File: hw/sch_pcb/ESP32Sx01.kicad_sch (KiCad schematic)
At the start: 33 parts, among them J1 HEADER_1x03, J2 USBC_USB4105-GF-A, J3 HEADER_1x12, J4 HEADER_1x12, J5 HEADER_1x12, J6 HEADER_1x03, J7 HEADER_1x03, J8 HEADER_2x05, Q1 BC817-25, SW1 434133025816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

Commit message: Update of PCB design
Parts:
- removed J7: HEADER_1x03, Mlab_Pin_Headers:Straight_2x03, symbol MLAB_HEADER:HEADER_2x03_PARALLEL
- Y1: footprint (none) -> Mlab_XTAL:ABS07
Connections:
- net +3V3: now also J4.21, J4.22
- net GND: now also J4.1, J4.19, J4.2, J4.20, J4.23, J4.24
- net GPIO12: now also J4.3, J4.4
- net GPIO13: now also J4.5, J4.6
- net GPIO14: now also J4.7, J4.8
- net GPIO17: now also J4.10, J4.9
- net GPIO18: now also J4.11, J4.12
- net GPIO21: now also J4.13, J4.14
- net GPIO35: no longer U3.31 (SPIIO6/GPIO35/FSPID/SUBSPID)
- net GPIO36: no longer U3.32 (SPIIO7/GPIO36/FSPICLK/SUBSPICLK)
- net GPIO37: no longer U3.33 (SPIDQS/GPIO37/FSPIQ/SUBSPIQ)
- net GPIO47: now also J4.15, J4.16
- net GPIO48: now also J4.17, J4.18
- net GPIO33: no longer names the net of U3.28 (SPIIO4/GPIO33/FSPIHD/SUBSPIHD)
- net GPIO34: no longer names the net of U3.29 (SPIIO5/GPIO34/FSPICS0/SUBSPICS0)
- no-connect marks 3 -> 8

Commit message: finishing PCB design
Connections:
- net GPIO35 is gone; now on net GND: J5.1, J5.2
- net GPIO36 is gone; now on net +3V3: J5.3, J5.4
- net GPIO37 is gone; now on net GND: J5.5, J5.6
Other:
- company: (none) -> MLAB
- title: (none) -> ESP32Sx01A
- moved on the sheet: C4, C5, Y1

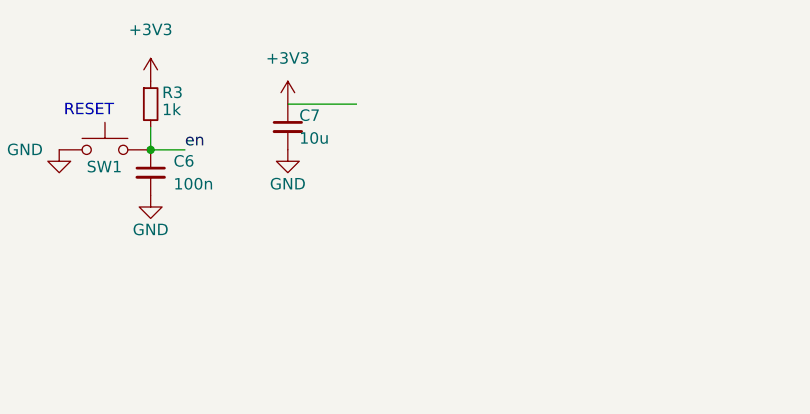
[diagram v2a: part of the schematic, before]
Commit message: move boot button
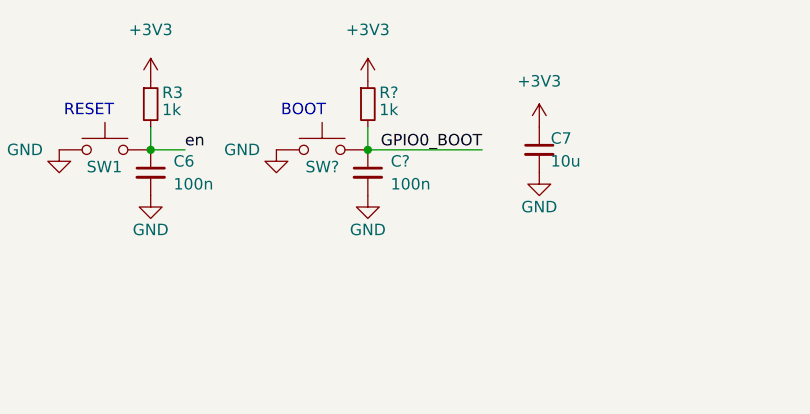
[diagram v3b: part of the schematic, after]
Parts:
- added C?: 100n, Capacitor_SMD:C_0805_2012Metric, symbol Device:C_Small
- added R?: 1k, Resistor_SMD:R_0805_2012Metric, symbol Device:R_Small
- added SW?: 434133025816, Button_Switch_SMD:SW_Push_1P1T_NO_Vertical_Wuerth_434133025816, symbol Switch:SW_Push
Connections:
- net +3V3: now also R?.1
- net GND: now also C?.2, SW?.1
- net GPIO0_BOOT: now also C?.1, R?.2, SW?.2
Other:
- note added: "BOOT"
- moved on the sheet: C7

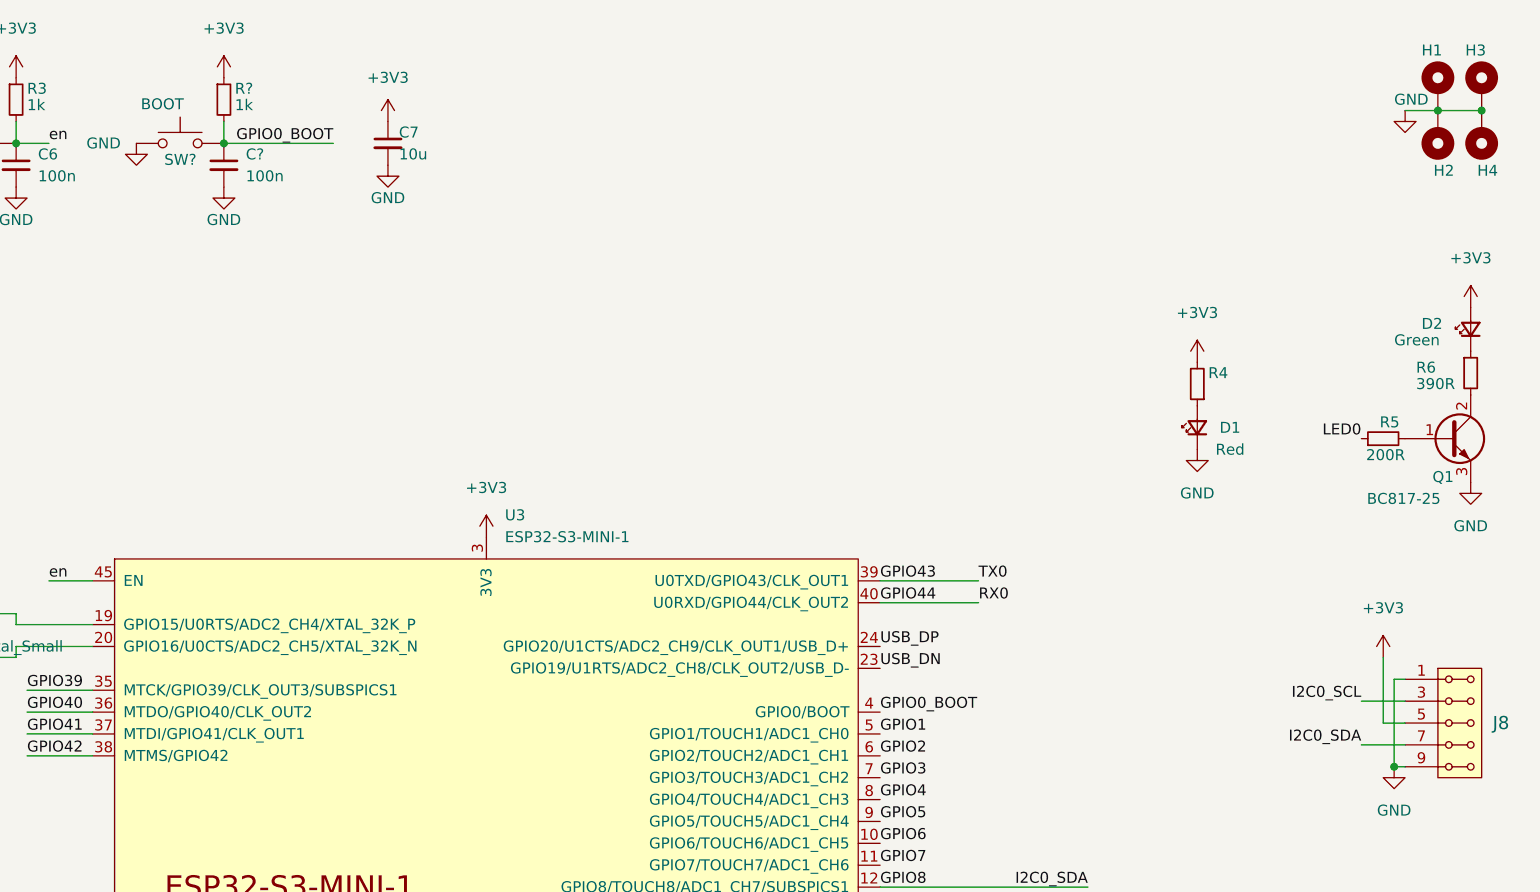
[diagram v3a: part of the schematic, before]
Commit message: solve missing anotation in schematics
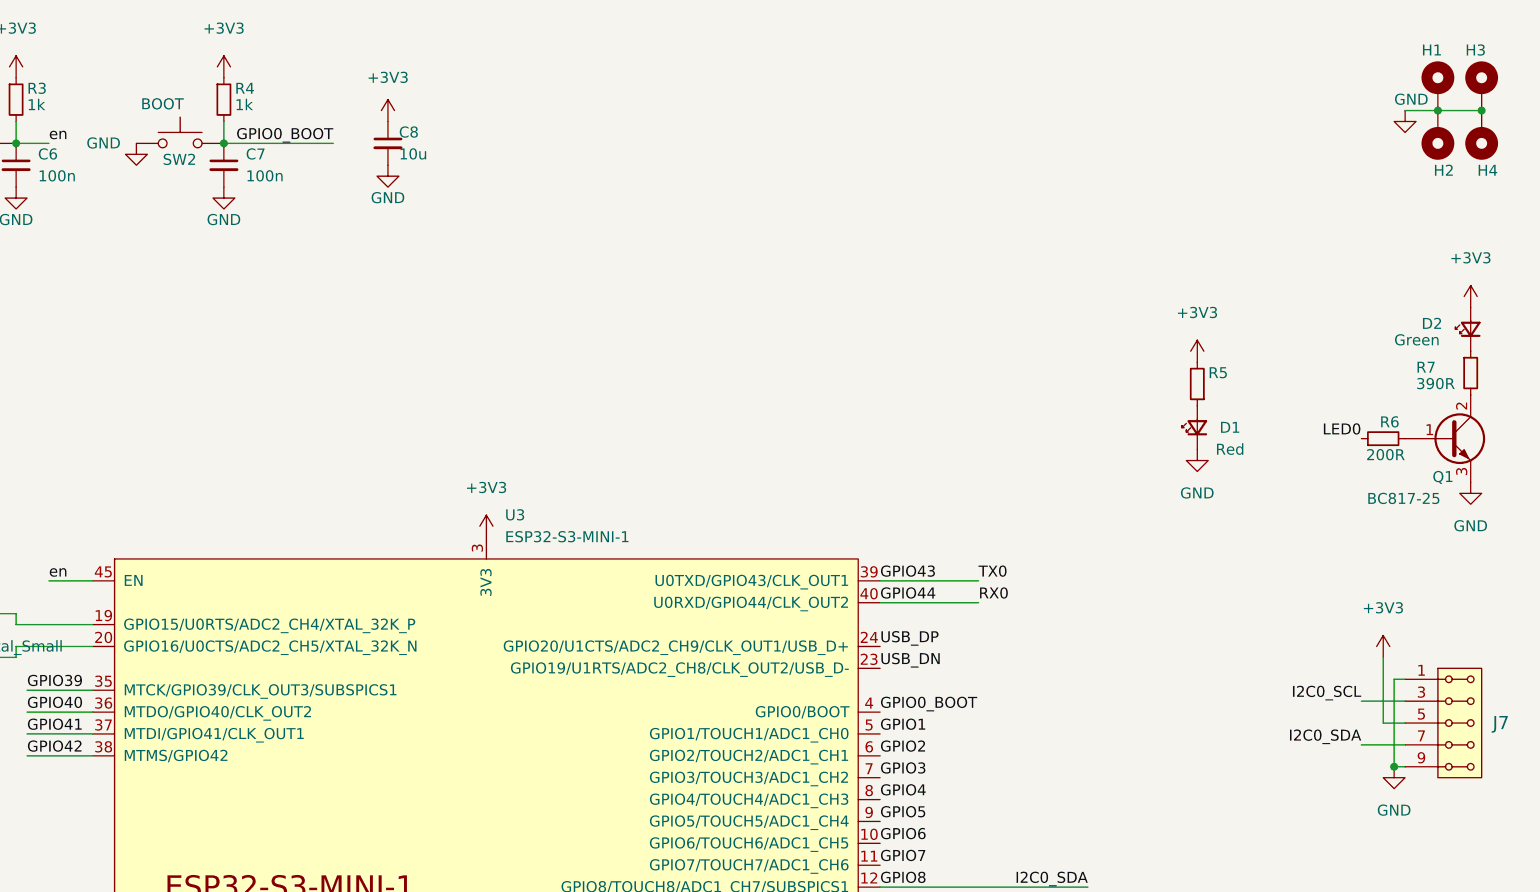
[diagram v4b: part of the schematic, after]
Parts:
- gave numbers to parts that had none: 3
- renumbered C7 to C8, J8 to J7, R4 to R5, R5 to R6, R6 to R7

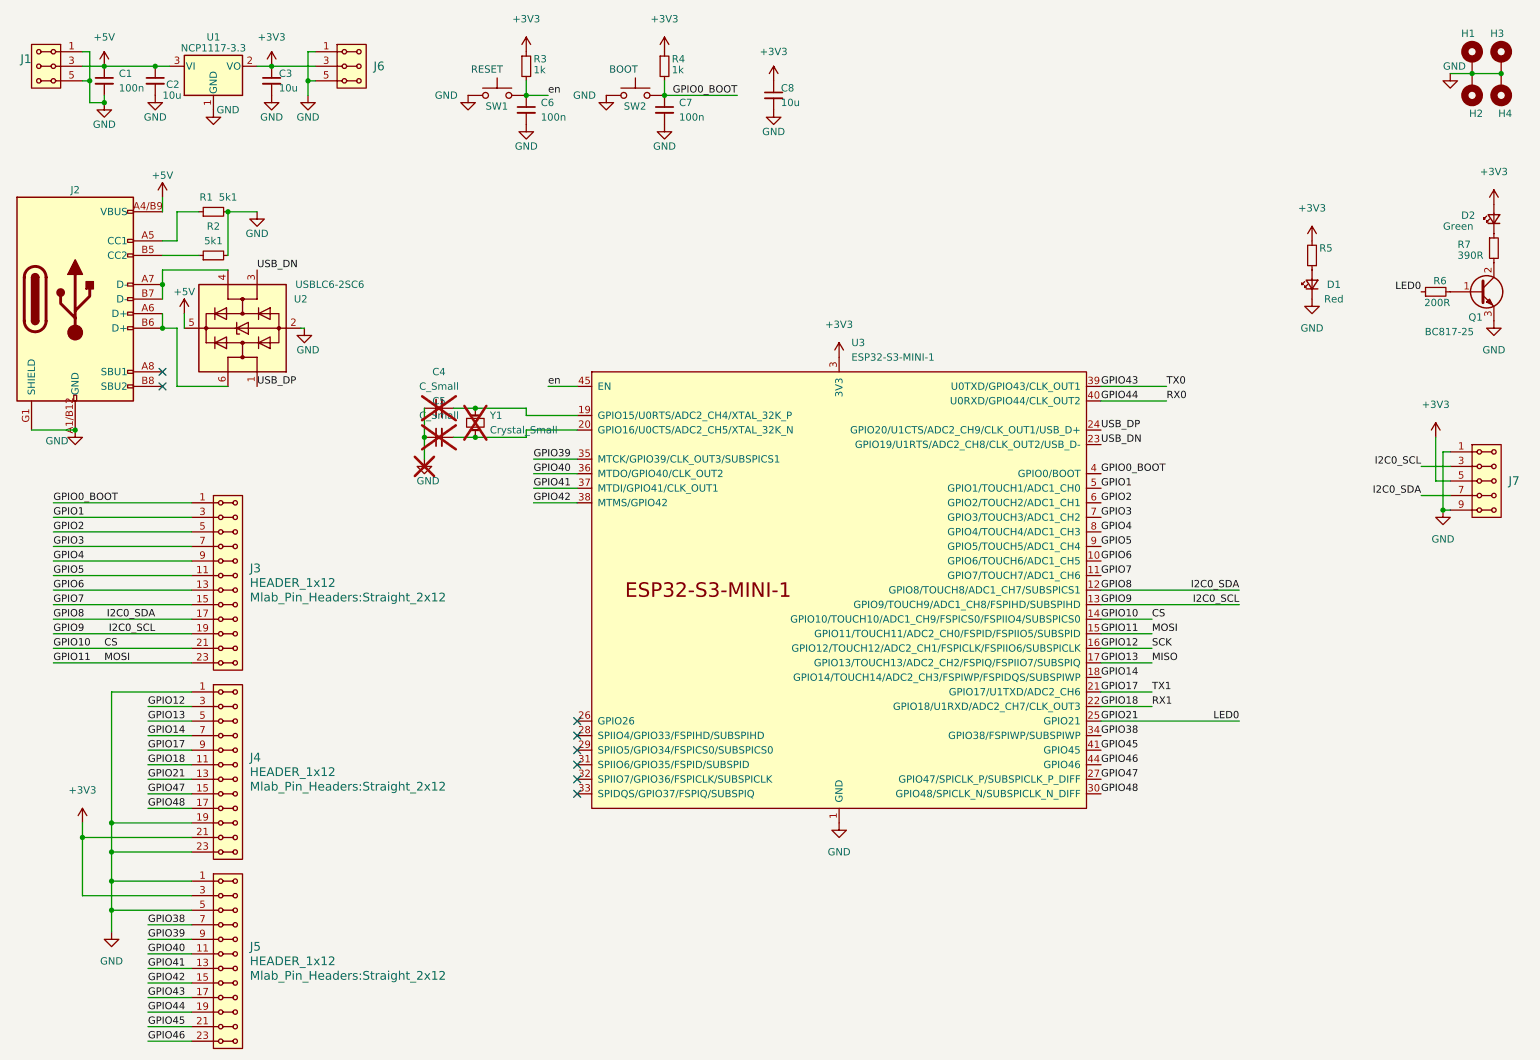
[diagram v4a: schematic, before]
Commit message: add polarity-swap protection
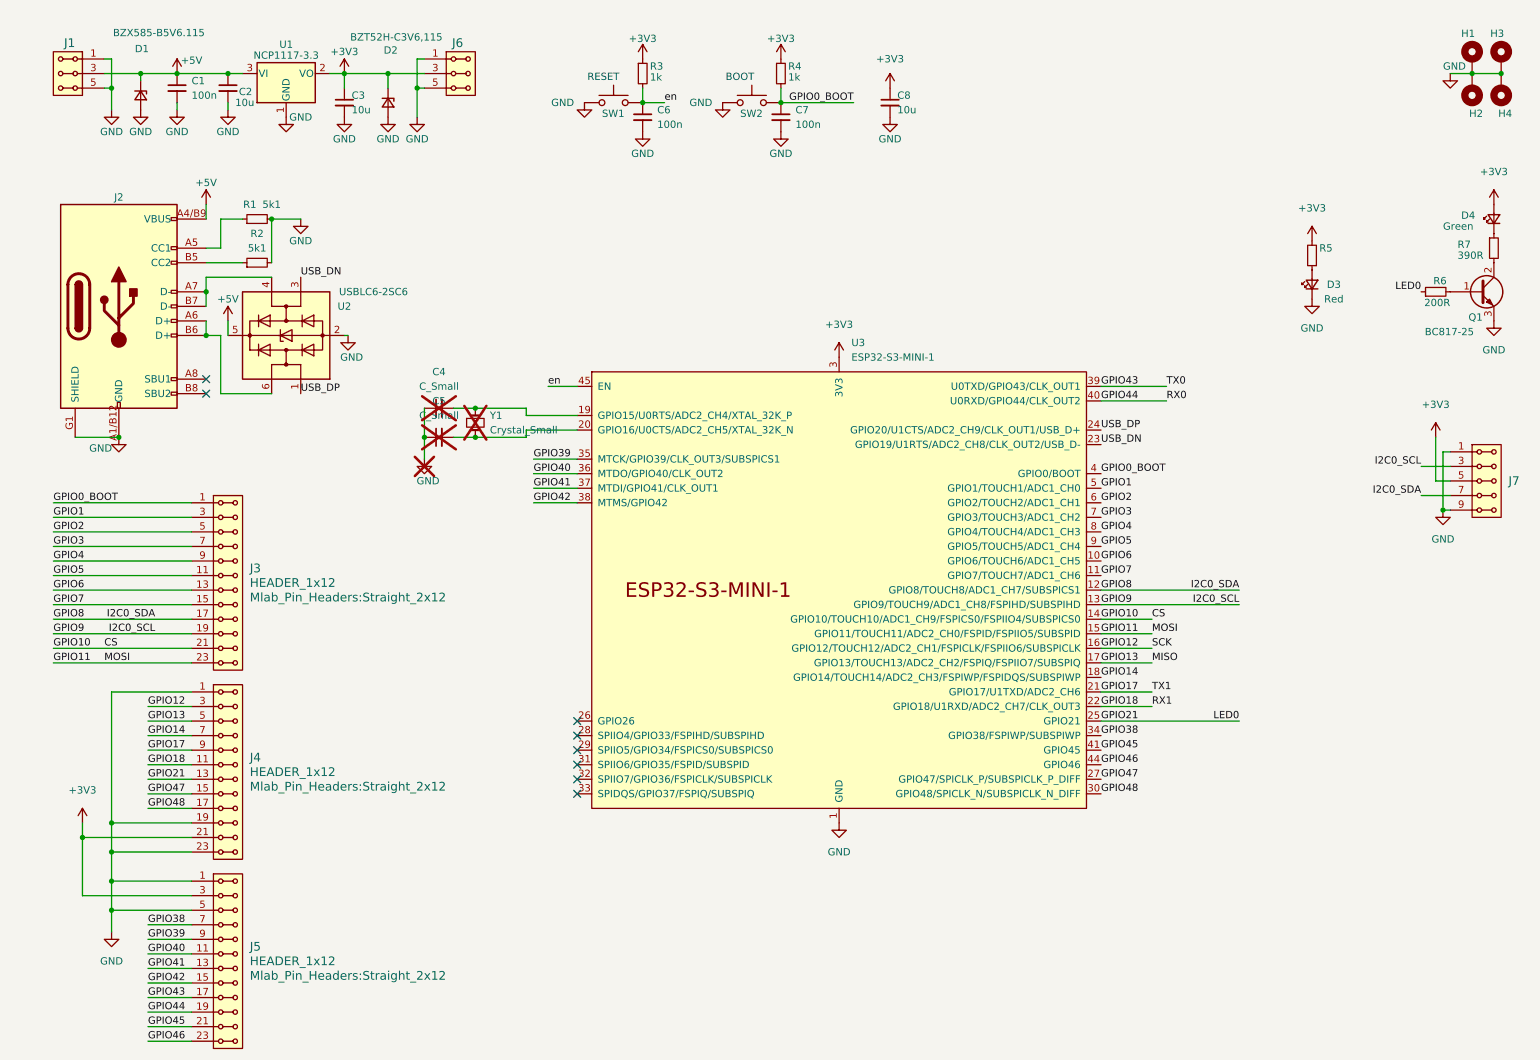
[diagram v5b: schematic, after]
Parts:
- added D1: BZX585-B5V6.115, Diode_SMD:D_SOD-523, symbol Device:D_Zener_Small
- added D2: BZT52H-C3V6,115, Diode_SMD:Nexperia_CFP3_SOD-123W, symbol Device:D_Zener_Small
- renumbered D1 to D3, D2 to D4
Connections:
- net +3V3: now also D2.1 (K)
- net +5V: now also D1.1 (K)
- net GND: now also D1.2 (A), D2.2 (A)
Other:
- moved on the sheet: C1, C2, C3, C6, C7, C8, J1, J2, J6, R1, R2, R3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

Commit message: Cleanup fab layer. Resolve DRC errors.
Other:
- company: MLAB -> MLAB.cz
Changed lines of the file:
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@@
 	(title_block
 		(title "ESP32Sx01A")
-		(date "2026")
-		(company "MLAB")
-		(comment 2 "roman-dvorak")
+		(date "2026-02-15")
+		(company "MLAB.cz")
+		(comment 1 " ESP32-S3 MLAB breakout board ")
+		(comment 3 "roman-dvorak")
 	)
 	(text "RESET"

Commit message: Update UST_IDs.
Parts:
- C1, C6, C7: UST_ID (none) -> 5c70984712875079b91f8b4c
- C2, C3, C8: UST_ID (none) -> 5c70984712875079b91f8b53
- C4, C5, Y1: now left out of the parts list
- D1: UST_ID (none) -> 60879d38128750769ee58e48
- D2: UST_ID (none) -> 650b35ab462c6d9e720543d0
- J2: UST_ID (none) -> 5fa0f94612875025b397795e
- Q1: UST_ID (none) -> 5c70984712875079b91f8aea
- R1, R2: UST_ID (none) -> 5fa0fc3e12875025b3977997
- R3, R4: UST_ID (none) -> 5c70984512875079b91f898c
- R5, R6: UST_ID (none) -> 5c70984512875079b91f897d
- R7: UST_ID (none) -> 5fa12b6012875025b3977a16
- SW1, SW2: UST_ID (none) -> 6998c49ed42e6e3c4d330f22
- U1: UST_ID (none) -> 5c70984712875079b91f8af9
- U2: UST_ID (none) -> 5e82e0691287502a334a778c
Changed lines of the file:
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@@
 			)
 		)
+		(property "UST_ID" "5fa0fc3e12875025b3977997"
+			(at 58.42 59.69 90)
+			(effects
+				(font
+					(size 1.27 1.27)
+				)
+				(hide yes)
+			)
+		)
 		(pin "1"
 		)
@@
 		(unit 1)
 		(exclude_from_sim no)
-		(in_bom yes)
+		(in_bom no)
 		(on_board yes)
 		(dnp yes)
-		(fields_autoplaced yes)
 		(property "Reference" "C5"
-			(at 90.1763 83.82 90)
+			(at 85.09 90.17 90)
 			(effects
 				(font
@@
 		)
 		(property "Value" "C_Small"
-			(at 90.1763 86.36 90)
+			(at 93.98 93.98 90)
 			(effects
 				(font
@@
 			)
 		)
+		(property "UST_ID" "5c70984512875079b91f898c"
+			(at 125.73 26.67 0)
+			(effects
+				(font
+					(size 1.27 1.27)
+				)
+				(hide yes)
+			)
+		)
 		(pin "1"
 		)
@@
 			)
 		)
+		(property "UST_ID" "650b35ab462c6d9e720543d0"
+			(at 81.28 31.75 90)
+			(effects
+				(font
+					(size 1.27 1.27)
+				)
+				(hide yes)
+			)
+		)
 		(pin "1"
 		)
@@
 			)
 		)
+		(property "UST_ID" "6998c49ed42e6e3c4d330f22"
+			(at 120.65 31.75 0)
+			(effects
+				(font
+					(size 1.27 1.27)
+				)
+				(hide yes)
+			)
+		)
 		(pin "1"
 		)
@@
 			)
 		)
+		(property "UST_ID" "5c70984712875079b91f8af9"
+			(at 63.5 26.67 0)
+			(effects
+				(font
+					(size 1.27 1.27)
+				)
+				(hide yes)
+			)
+		)
 		(pin "1"
 		)
@@
 			)
 		)
+		(property "UST_ID" "5c70984712875079b91f8b53"
+			(at 168.91 31.75 0)
+			(effects
+				(font
+					(size 1.27 1.27)
+				)
+				(hide yes)
+			)
+		)
 		(pin "1"
 		)
@@
 			)
 		)
+		(property "UST_ID" "5c70984512875079b91f898c"
+			(at 149.86 26.67 0)
+			(effects
+				(font
+					(size 1.27 1.27)
+				)
+				(hide yes)
+			)
+		)
 		(pin "1"
 		)
@@
 			)
 		)
+		(property "UST_ID" "5c70984712875079b91f8b53"
+			(at 53.34 29.21 0)
+			(effects
+				(font
+					(size 1.27 1.27)
+				)
+				(hide yes)
+			)
+		)
 		(pin "1"
 		)
@@
 			)
 		)
+		(property "UST_ID" "5c70984712875079b91f8b4c"
+			(at 44.45 29.21 0)
+			(effects
+				(font
+					(size 1.27 1.27)
+				)
+				(hide yes)
+			)
+		)
 		(pin "1"
 		)
@@
 			)
 		)
+		(property "UST_ID" "5c70984512875079b91f897d"
+			(at 264.16 64.77 90)
+			(effects
+				(font
+					(size 1.27 1.27)
+				)
+				(hide yes)
+			)
+		)
 		(pin "1"
 		)
@@
 			)
 		)
+		(property "UST_ID" "5c70984712875079b91f8b4c"
+			(at 149.86 34.29 0)
+			(effects
+				(font
+					(size 1.27 1.27)
+				)
+				(hide yes)
+			)
+		)
 		(pin "1"
 		)
@@
 			)
 		)
+		(property "UST_ID" "5c70984512875079b91f897d"
+			(at 242.57 58.42 0)
+			(effects
+				(font
+					(size 1.27 1.27)
+				)
+				(hide yes)
+			)
+		)
 		(pin "1"
 		)
@@
 		(unit 1)
 		(exclude_from_sim no)
-		(in_bom yes)
+		(in_bom no)
 		(on_board yes)
 		(dnp yes)
-		(fields_autoplaced yes)
 		(property "Reference" "Y1"
-			(at 99.06 86.3599 90)
+			(at 100.33 87.63 90)
 			(effects
 				(font
@@
 		)
 		(property "Value" "Crystal_Small"
-			(at 99.06 88.8999 90)
+			(at 100.33 91.44 0)
 			(effects
 				(font
@@
 			)
 		)
+		(property "UST_ID" "5fa12b6012875025b3977a16"
+			(at 274.32 57.15 0)
+			(effects
+				(font
+					(size 1.27 1.27)
+				)
+				(hide yes)
+			)
+		)
 		(pin "1"
 		)
@@
 			)
 		)
+		(property "UST_ID" "5e82e0691287502a334a778c"
+			(at 63.5 72.39 90)
+			(effects
+				(font
+					(size 1.27 1.27)
+				)
+				(hide yes)
+			)
+		)
 		(pin "1"
 		)
@@
 			)
 		)
+		(property "UST_ID" "5c70984712875079b91f8b4c"
+			(at 125.73 34.29 0)
+			(effects
+				(font
+					(size 1.27 1.27)
+				)
+				(hide yes)
+			)
+		)
 		(pin "1"
 		)
@@
 			)
 		)
+		(property "UST_ID" "5c70984712875079b91f8b53"
+			(at 73.66 31.75 0)
+			(effects
+				(font
+					(size 1.27 1.27)
+				)
+				(hide yes)
+			)
+		)
 		(pin "1"
 		)
@@
 			)
 		)
+		(property "UST_ID" "5c70984712875079b91f8aea"
+			(at 271.78 64.77 0)
+			(effects
+				(font
+					(size 1.27 1.27)
+				)
+				(hide yes)
+			)
+		)
 		(pin "1"
 		)
@@
 		(unit 1)
 		(exclude_from_sim no)
-		(in_bom yes)
+		(in_bom no)
 		(on_board yes)
 		(dnp yes)
-		(fields_autoplaced yes)
 		(property "Reference" "C4"
-			(at 90.1763 78.74 90)
+			(at 85.09 85.09 90)
 			(effects
 				(font
@@
 		)
 		(property "Value" "C_Small"
-			(at 90.1763 81.28 90)
+			(at 95.25 82.55 90)
 			(effects
 				(font
@@
 			)
 		)
+		(property "UST_ID" "6998c49ed42e6e3c4d330f22"
+			(at 144.78 31.75 0)
+			(effects
+				(font
+					(size 1.27 1.27)
+				)
+				(hide yes)
+			)
+		)
 		(pin "1"
 		)
@@
 			)
 		)
+		(property "UST_ID" "5fa0f94612875025b397795e"
+			(at 34.29 67.31 0)
+			(effects
+				(font
+					(size 1.27 1.27)
+				)
+				(hide yes)
+			)
+		)
 		(pin "A1/B12"
 		)
@@
 			)
 		)
+		(property "UST_ID" "5fa0fc3e12875025b3977997"
+			(at 58.42 52.07 90)
+			(effects
+				(font
+					(size 1.27 1.27)
+				)
+				(hide yes)
+			)
+		)
 		(pin "1"
 		)
@@
 			(effects
 				(font
+					(size 1.27 1.27)
+				)
+				(hide yes)
+			)
+		)
+		(property "UST_ID" "60879d38128750769ee58e48"
+			(at 38.1 30.48 90)
+			(effects
+				(font

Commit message: Add UST_ID for Y1.
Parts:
- Y1: value Crystal_Small -> 32.768kHz; UST_ID (none) -> 5c70984712875079b91f8b1b
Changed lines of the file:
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@@
 			)
 		)
-		(property "Value" "Crystal_Small"
+		(property "Value" "32.768kHz"
 			(at 100.33 91.44 0)
 			(effects
@@
 		)
 		(property "Description" "Two pin crystal, small symbol"
+			(at 96.52 87.63 0)
+			(effects
+				(font
+					(size 1.27 1.27)
+				)
+				(hide yes)
+			)
+		)
+		(property "UST_ID" "5c70984712875079b91f8b1b"
 			(at 96.52 87.63 0)
 			(effects
@@
 		(in_bom yes)
 		(on_board yes)
-		(dnp yes)
+		(dnp no)
 		(property "Reference" "#PWR018"
 			(at 87.63 100.33 0)
@@
 			(at 87.63 93.98 0)
 			(effects
+				(font
+					(size 1.27 1.27)
+				)
+				(hide yes)
+			)
+		)
+		(property "UST_ID" ""
+			(at 87.63 93.98 0)
+			(effects
